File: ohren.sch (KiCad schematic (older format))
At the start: 18 parts

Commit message: Add LEDs and drivers
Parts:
- removed D10, D11, D12, D13, D14, D15, D2, D3, D4, D5, D6, D7, D8, D9: WS2812B, LED_SMD:LED_WS2812B_PLCC4_5.0x5.0mm_P3.2mm, symbol LED:WS2812B
- removed U?: TLC5951RHA, Package_DFN_QFN:Texas_S-PVQFN-N40_EP4.15x4.15mm_ThermalVias, symbol Driver_LED:TLC5951RHA
- added C2, C4: CP, symbol Device:CP
- added C3: C, Capacitor_SMD:C_0805_2012Metric, symbol Device:C
- added D10, D11, D12, D13, D14, D15, D16, D17, D2, D3, D4, D5, D6, D7, D8, D9: LED_ARGB, LED_SMD:LED_Cree-PLCC4_3.2x2.8mm_CCW, symbol Device:LED_ARGB
- added U2: TLC5951RHA, Package_DFN_QFN:Texas_S-PVQFN-N40_EP4.15x4.15mm_ThermalVias, symbol Driver_LED:TLC5951RHA
- C1: footprint LED_SMD:LED_0402_1005Metric -> Capacitor_SMD:C_0805_2012Metric
- gave numbers to parts that had none: 1
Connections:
- net labels added: DCSCHAIN, DCSCK, GND, GSCKB, GSCKG, GSCKR, GSLAT, GSSCHAIN, GSSCK, U1_B0, U1_B1, U1_B2, U1_B3, U1_B4, U1_B5, U1_B6, U1_B7, U1_G0, U1_G1, U1_G2, U1_G3, U1_G4, U1_G5, U1_G6, U1_G7, U1_R0, U1_R1, U1_R2, U1_R3, U1_R4, U1_R5, U1_R6, U1_R7, U2_B0, U2_B1, U2_B2, U2_B3, U2_B4, U2_B5, U2_B6, U2_B7, U2_G0, U2_G1, U2_G2, U2_G3, U2_G4, U2_G5, U2_G6, U2_G7, U2_R0, U2_R1, U2_R2, U2_R3, U2_R4, U2_R5, U2_R6, U2_R7, VCC, VDD, XBLINK
- wire segments 0 -> 158
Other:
- moved on the sheet: D1

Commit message: Route
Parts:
- added C5, C6, C7, C8: C, Capacitor_SMD:C_1210_3225Metric, symbol Device:C
- added J1: Conn_01x14_Male, catear-pcb:solder_conn14, symbol Connector:Conn_01x14_Male
- U1, U2: symbol Driver_LED:TLC5951RHA -> ohren-rescue:TLC5951RHA-Driver_LED
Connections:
- net labels added: DCSIN, DCSOUT, GSSIN, GSSOUT, XBLNK
- net labels removed: XBLINK
- wire segments 158 -> 202
- no-connect marks 0 -> 1
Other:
- moved on the sheet: C1, C2, C3, C4, D1, D10, D11, D12, D13, D14, D15, D16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

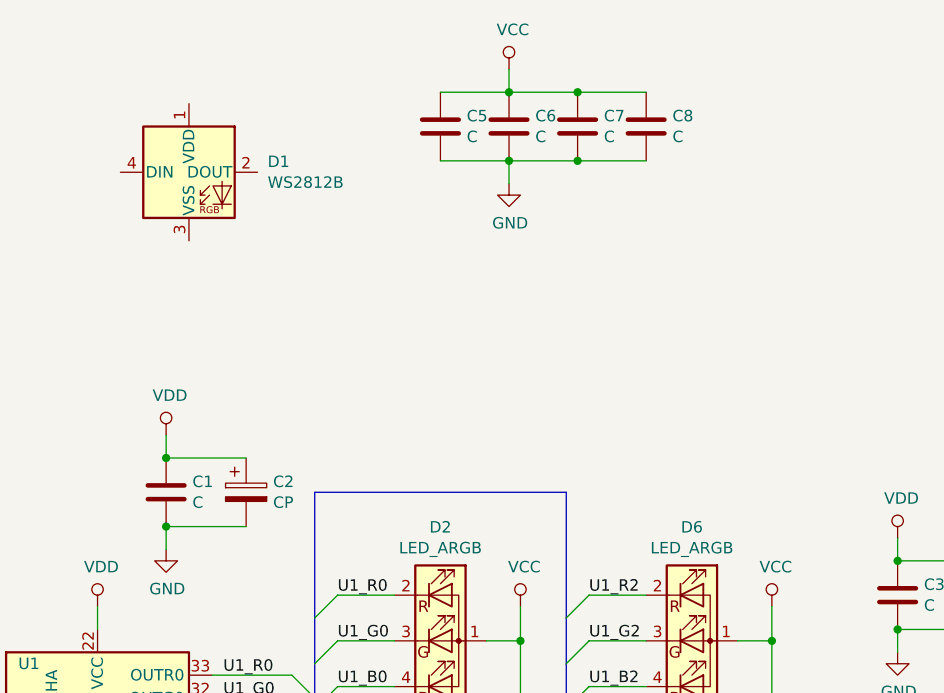
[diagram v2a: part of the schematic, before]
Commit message: Add some bypass capacitance
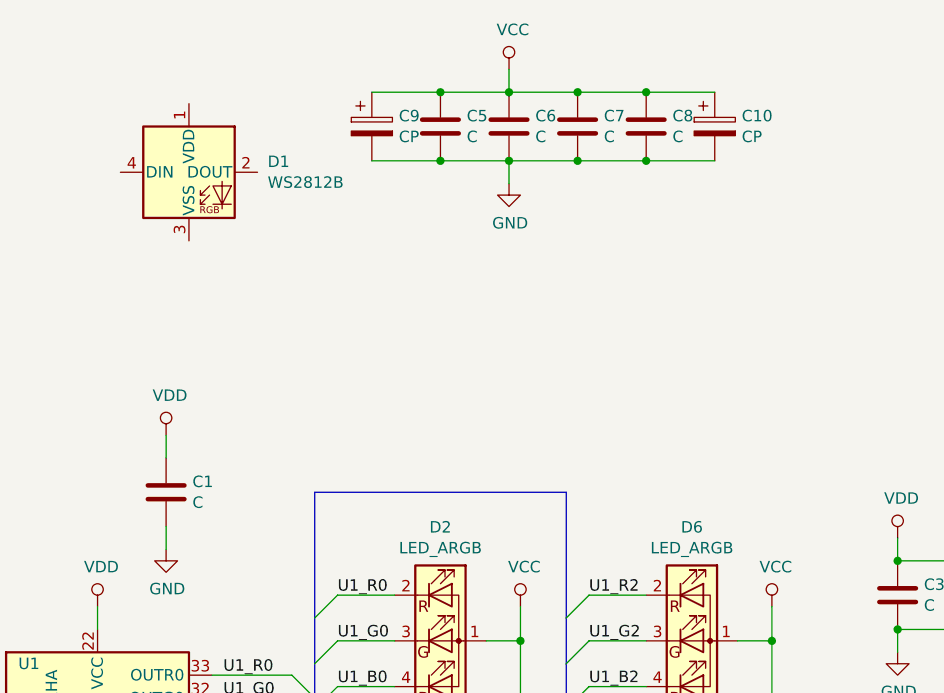
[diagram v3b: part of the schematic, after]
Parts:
- removed C2: CP, symbol Device:CP
- added C10, C9: CP, Capacitor_Tantalum_SMD:CP_EIA-6032-28_Kemet-C, symbol Device:CP
- C4: footprint (none) -> Capacitor_Tantalum_SMD:CP_EIA-6032-28_Kemet-C
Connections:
- net GND: now also C10.2, C9.2
- net VCC: now also C10.1, C9.1
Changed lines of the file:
@@
 Wire Wire Line
 	3350 6150 3350 6250
-Connection ~ 3650 2900
-Wire Wire Line
-	4000 2900 3650 2900
-Connection ~ 3650 2600
-Wire Wire Line
-	4000 2600 3650 2600
-$Comp
-L Device:CP C2
-U 1 1 5C9AA679
-P 4000 2750
-F 0 "C2" H 4118 2796 50  0000 L CNN
-F 1 "CP" H 4118 2705 50  0000 L CNN
-F 2 "" H 4038 2600 50  0001 C CNN
-F 3 "~" H 4000 2750 50  0001 C CNN
-	1    4000 2750
-	1    0    0    -1
-$EndComp
 Wire Wire Line
 	3650 2900 3650 3000
@@
 F 0 "C4" H 7318 3246 50  0000 L CNN
 F 1 "CP" H 7318 3155 50  0000 L CNN
-F 2 "" H 7238 3050 50  0001 C CNN
+F 2 "Capacitor_Tantalum_SMD:CP_EIA-6032-28_Kemet-C" H 7238 3050 50  0001 C CNN
 F 3 "~" H 7200 3200 50  0001 C CNN
 	1    7200 3200
@@
 Wire Wire Line
 	1400 3450 1400 2500
+$Comp
+L Device:CP C9
+U 1 1 5D009474
+P 4550 1150
+F 0 "C9" H 4668 1196 50  0000 L CNN
+F 1 "CP" H 4668 1105 50  0000 L CNN
+F 2 "Capacitor_Tantalum_SMD:CP_EIA-6032-28_Kemet-C" H 4588 1000 50  0001 C CNN
+F 3 "~" H 4550 1150 50  0001 C CNN
+	1    4550 1150
+	1    0    0    -1
+$EndComp
+$Comp
+L Device:CP C10
+U 1 1 5D01A6A4
+P 6050 1150
+F 0 "C10" H 6168 1196 50  0000 L CNN
+F 1 "CP" H 6168 1105 50  0000 L CNN
+F 2 "Capacitor_Tantalum_SMD:CP_EIA-6032-28_Kemet-C" H 6088 1000 50  0001 C CNN
+F 3 "~" H 6050 1150 50  0001 C CNN
+	1    6050 1150
+	1    0    0    -1
+$EndComp
+Wire Wire Line
+	6050 1000 5750 1000
+Connection ~ 5750 1000
+Wire Wire Line
+	6050 1300 5750 1300
+Connection ~ 5750 1300
+Wire Wire Line
+	4850 1000 4550 1000
+Connection ~ 4850 1000
+Wire Wire Line
+	4850 1300 4550 1300
 Wire Bus Line
 	5400 2750 5400 4550
@@
 Wire Bus Line
 	2350 2650 2350 6850
+Connection ~ 4850 1300
 $EndSCHEMATC

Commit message: Partial reroute
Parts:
- removed D1: WS2812B, LED_SMD:LED_WS2812B_PLCC4_5.0x5.0mm_P3.2mm, symbol LED:WS2812B
- removed D13, D16, D2, D3: LED_ARGB, LED_SMD:LED_Cree-PLCC4_3.2x2.8mm_CCW, symbol Device:LED_ARGB
- added D19, D20, D21, D22, D23, D24, D25, D26: LED, catear-pcb:smd_led_universal, symbol Device:LED
- added R1, R2: 2k4, Resistor_SMD:R_0402_1005Metric, symbol Device:R
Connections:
- wire segments 204 -> 227
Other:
- moved on the sheet: D10, D11, D12, D14, D17, D4, D6, D7

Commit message: Reroute finised
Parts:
- removed C4: CP, Capacitor_Tantalum_SMD:CP_EIA-6032-28_Kemet-C, symbol Device:CP
- C10, C9: value CP -> C; footprint Capacitor_Tantalum_SMD:CP_EIA-6032-28_Kemet-C -> Capacitor_SMD:C_1206_3216Metric; symbol Device:CP -> Device:C
- J1: value Conn_01x14_Male -> Conn_01x18_Male; footprint catear-pcb:solder_conn14 -> catear-pcb:solder_conn18; symbol Connector:Conn_01x14_Male -> Connector:Conn_01x18_Male
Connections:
- wire segments 227 -> 242
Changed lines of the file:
@@
 Wire Wire Line
 	7850 6150 7850 6200
-Connection ~ 6850 3350
-Wire Wire Line
-	7200 3350 6850 3350
-Connection ~ 6850 3050
-Wire Wire Line
-	7200 3050 6850 3050
-$Comp
-L Device:CP C4
-U 1 1 5CA31CE6
-P 7200 3200
-F 0 "C4" H 7318 3246 50  0000 L CNN
-F 1 "CP" H 7318 3155 50  0000 L CNN
-F 2 "Capacitor_Tantalum_SMD:CP_EIA-6032-28_Kemet-C" H 7238 3050 50  0001 C CNN
-F 3 "~" H 7200 3200 50  0001 C CNN
-	1    7200 3200
-	1    0    0    -1
-$EndComp
 Wire Wire Line
 	6850 3350 6850 3450
@@
 	1    0    0    -1
 $EndComp
-NoConn ~ 2000 2300
+NoConn ~ 2000 2700
 Wire Wire Line
 	5150 1300 5150 1400
@@
 	1    0    0    -1
 $EndComp
-Wire Wire Line
-	400  2500 400  3200
-$Comp
-L power:GND #PWR0119
-U 1 1 5CC0E0FA
-P 400 3200
-F 0 "#PWR0119" H 400 2950 50  0001 C CNN
-F 1 "GND" H 405 3027 50  0000 C CNN
-F 2 "" H 400 3200 50  0001 C CNN
-F 3 "" H 400 3200 50  0001 C CNN
-	1    400  3200
-	1    0    0    -1
-$EndComp
 $Comp
 L power:VCC #PWR0120
 U 1 1 5CC1AB18
-P 0 2250
-F 0 "#PWR0120" H 0   2100 50  0001 C CNN
-F 1 "VCC" H 17  2423 50  0000 C CNN
-F 2 "" H 0   2250 50  0001 C CNN
-F 3 "" H 0   2250 50  0001 C CNN
-	1    0    2250
-	1    0    0    -1
-$EndComp
-Wire Wire Line
-	0    2250 0    2500
-$Comp
-L power:GND #PWR0121
-U 1 1 5CC4100A
-P 2550 2600
-F 0 "#PWR0121" H 2550 2350 50  0001 C CNN
-F 1 "GND" H 2555 2427 50  0000 C CNN
-F 2 "" H 2550 2600 50  0001 C CNN
-F 3 "" H 2550 2600 50  0001 C CNN
-	1    2550 2600
-	1    0    0    -1
-$EndComp
-Wire Wire Line
-	2550 2600 2550 2500
-Wire Wire Line
-	2550 2500 1500 2500
-Entry Wire Line
-	2250 2750 2350 2650
-Entry Wire Line
-	2250 2850 2350 2750
-Entry Wire Line
-	2250 2950 2350 2850
-Entry Wire Line
-	2250 3050 2350 2950
+P -850 2250
+F 0 "#PWR0120" H -850 2100 50  0001 C CNN
+F 1 "VCC" H -833 2423 50  0000 C CNN
+F 2 "" H -850 2250 50  0001 C CNN
+F 3 "" H -850 2250 50  0001 C CNN
+	1    -850 2250
+	1    0    0    -1
+$EndComp
 Entry Wire Line
 	2250 3150 2350 3050
@@
 Entry Wire Line
 	2250 3750 2350 3650
-Text Label 1800 2850 0    50   ~ 0
+Entry Wire Line
+	2250 3850 2350 3750
+Entry Wire Line
+	2250 3950 2350 3850
+Entry Wire Line
+	2250 4050 2350 3950
+Entry Wire Line
+	2250 4150 2350 4050
+Text Label 1800 4150 0    50   ~ 0
 GSSOUT
-Text Label 1800 2750 0    50   ~ 0
+Text Label 1800 4050 0    50   ~ 0
 DCSOUT
-Text Label 1800 2950 0    50   ~ 0
+Text Label 1800 3450 0    50   ~ 0
 GSSIN
-Text Label 1800 3050 0    50   ~ 0
+Text Label 1800 3350 0    50   ~ 0
 DCSIN
-Text Label 1800 3150 0    50   ~ 0
+Text Label 1800 3550 0    50   ~ 0
 GSSCK
 Text Label 1800 3250 0    50   ~ 0
-GSLAT
-Text Label 1800 3350 0    50   ~ 0
 DCSCK
-Text Label 1800 3450 0    50   ~ 0
+Text Label 1800 3150 0    50   ~ 0
 XBLNK
-Text Label 1800 3550 0    50   ~ 0
+Text Label 1800 3750 0    50   ~ 0
 GSCKR
-Wire Wire Line
-	0    2500 200  2500
-$Comp
-L Connector:Conn_01x14_Male J1
-U 1 1 5CDF8D04
-P 900 2300
-F 0 "J1" V 735 2228 50  0000 C CNN
-F 1 "Conn_01x14_Male" V 826 2228 50  0000 C CNN
-F 2 "catear-pcb:solder_conn14" H 900 2300 50  0001 C CNN
-F 3 "~" H 900 2300 50  0001 C CNN
-	1    900  2300
-	0    1    1    0
-$EndComp
-Connection ~ 200  2500
-Wire Wire Line
-	200  2500 300  2500
-Wire Wire Line
-	-200 2600 -200 2250
-$Comp
-L power:VDD #PWR0122
-U 1 1 5CE5FD09
-P -200 2250
-F 0 "#PWR0122" H -200 2100 50  0001 C CNN
-F 1 "VDD" H -183 2423 50  0000 C CNN
-F 2 "" H -200 2250 50  0001 C CNN
-F 3 "" H -200 2250 50  0001 C CNN
-	1    -200 2250
-	1    0    0    -1
-$EndComp
-Wire Wire Line
-	2250 3650 600  3650
-Wire Wire Line
-	600  3650 600  3550
-Wire Wire Line
-	2250 3750 600  3750
-Wire Wire Line
-	600  3750 600  3650
-Connection ~ 600  3650
-Text Label 1800 3650 0    50   ~ 0
+Text Label 1800 3850 0    50   ~ 0
 GSCKG
-Text Label 1800 3750 0    50   ~ 0
+Text Label 1800 3950 0    50   ~ 0
 GSCKB
 Entry Wire Line
@@
 Entry Wire Line
 	2350 4350 2450 4250
-Wire Wire Line
-	500  3050 2250 3050
-Wire Wire Line
-	500  2500 500  3050
-Wire Wire Line
-	600  2950 600  2500
-Wire Wire Line
-	600  2950 2250 2950
-Wire Wire Line
-	600  3550 1000 3550
-Wire Wire Line
-	700  2850 700  2500
-Wire Wire Line
-	700  2850 2250 2850
-Wire Wire Line
-	800  2750 800  2500
-Wire Wire Line
-	800  2750 2250 2750
-Wire Wire Line
-	-200 2600 900  2600
-Wire Wire Line
-	900  2600 900  2500
-Wire Wire Line
-	1000 2500 1000 3550
-Connection ~ 1000 3550
-Wire Wire Line
-	1000 3550 2250 3550
-Wire Wire Line
-	2250 3250 1100 3250
-Wire Wire Line
-	1100 3250 1100 2500
-Wire Wire Line
-	2250 3150 1200 3150
-Wire Wire Line
-	1200 3150 1200 2500
-Wire Wire Line
-	2250 3350 1300 3350
-Wire Wire Line
-	1300 3350 1300 2500
-Wire Wire Line
-	2250 3450 1400 3450
-Wire Wire Line
-	1400 3450 1400 2500
-$Comp
-L Device:CP C9
+$Comp
+L Device:C C9
 U 1 1 5D009474
 P 4550 1150
 F 0 "C9" H 4668 1196 50  0000 L CNN
-F 1 "CP" H 4668 1105 50  0000 L CNN
-F 2 "Capacitor_Tantalum_SMD:CP_EIA-6032-28_Kemet-C" H 4588 1000 50  0001 C CNN
+F 1 "C" H 4668 1105 50  0000 L CNN
+F 2 "Capacitor_SMD:C_1206_3216Metric" H 4588 1000 50  0001 C CNN
 F 3 "~" H 4550 1150 50  0001 C CNN
 	1    4550 1150
@@
 $EndComp
 $Comp
-L Device:CP C10
+L Device:C C10
 U 1 1 5D01A6A4
 P 6050 1150
 F 0 "C10" H 6168 1196 50  0000 L CNN
-F 1 "CP" H 6168 1105 50  0000 L CNN
-F 2 "Capacitor_Tantalum_SMD:CP_EIA-6032-28_Kemet-C" H 6088 1000 50  0001 C CNN
+F 1 "C" H 6168 1105 50  0000 L CNN
+F 2 "Capacitor_SMD:C_1206_3216Metric" H 6088 1000 50  0001 C CNN
 F 3 "~" H 6050 1150 50  0001 C CNN
 	1    6050 1150
@@
 Wire Wire Line
 	2800 1500 2800 1750
+Text Label 3100 1750 1    50   ~ 0
+U2_G1
+Wire Wire Line
+	3100 1500 3100 1750
+Text Label 2500 1750 1    50   ~ 0
+U2_R1
+Wire Wire Line
+	2500 1500 2500 1750
+$Comp
+L Connector:Conn_01x18_Male J1
+U 1 1 5CDF8D04
+P 550 2200
+F 0 "J1" V 385 2128 50  0000 C CNN
+F 1 "Conn_01x18_Male" V 476 2128 50  0000 C CNN
+F 2 "catear-pcb:solder_conn18" H 550 2200 50  0001 C CNN
+F 3 "~" H 550 2200 50  0001 C CNN
+	1    550  2200
+	0    1    1    0
+$EndComp
+Wire Wire Line
+	-350 2400 -350 2550
+Wire Wire Line
+	-350 2550 -850 2550
+Wire Wire Line
+	-850 2550 -850 2250
+Wire Wire Line
+	-350 2550 -250 2550
+Wire Wire Line
+	-250 2550 -250 2400
+Connection ~ -350 2550
+$Comp
+L power:VCC #PWR0119
+U 1 1 5CD6CF6B
+P 1800 2250
+F 0 "#PWR0119" H 1800 2100 50  0001 C CNN
+F 1 "VCC" H 1817 2423 50  0000 C CNN
+F 2 "" H 1800 2250 50  0001 C CNN
+F 3 "" H 1800 2250 50  0001 C CNN
+	1    1800 2250
+	1    0    0    -1
+$EndComp
+Wire Wire Line
+	1800 2550 1800 2250
+Wire Wire Line
+	1800 2550 1350 2550
+Wire Wire Line
+	1250 2550 1250 2400
+Wire Wire Line
+	1350 2400 1350 2550
+Connection ~ 1350 2550
+Wire Wire Line
+	1350 2550 1250 2550
+Wire Wire Line
+	-150 2400 -150 2650
+Wire Wire Line
+	-150 2650 -850 2650
+Wire Wire Line
+	-50  2400 -50  2650
+Wire Wire Line
+	-50  2650 -150 2650
+Connection ~ -150 2650
+$Comp
+L power:GND #PWR0121
+U 1 1 5CDDA28F
+P -850 2750
+F 0 "#PWR0121" H -850 2500 50  0001 C CNN
+F 1 "GND" H -845 2577 50  0000 C CNN
+F 2 "" H -850 2750 50  0001 C CNN
+F 3 "" H -850 2750 50  0001 C CNN
+	1    -850 2750
+	1    0    0    -1
+$EndComp
+Wire Wire Line
+	-850 2750 -850 2650
+$Comp
+L power:GND #PWR0124
+U 1 1 5CDEC54B
+P 1800 2850
+F 0 "#PWR0124" H 1800 2600 50  0001 C CNN
+F 1 "GND" H 1805 2677 50  0000 C CNN
+F 2 "" H 1800 2850 50  0001 C CNN
+F 3 "" H 1800 2850 50  0001 C CNN
+	1    1800 2850
+	1    0    0    -1
+$EndComp
+Wire Wire Line
+	1800 2850 1800 2750
+Wire Wire Line
+	1800 2750 1150 2750
+Connection ~ 1150 2750
+Wire Wire Line
+	1150 2750 1050 2750
+$Comp
+L power:VDD #PWR0122
+U 1 1 5CE3A90D
+P 2000 2250
+F 0 "#PWR0122" H 2000 2100 50  0001 C CNN
+F 1 "VDD" H 2017 2423 50  0000 C CNN
+F 2 "" H 2000 2250 50  0001 C CNN
+F 3 "" H 2000 2250 50  0001 C CNN
+	1    2000 2250
+	1    0    0    -1
+$EndComp
+Wire Wire Line
+	1150 2400 1150 2750
+Wire Wire Line
+	1050 2400 1050 2750
+Wire Wire Line
+	2000 2650 950  2650
+Wire Wire Line
+	950  2650 950  2400
+Wire Wire Line
+	2000 2250 2000 2650
+Wire Wire Line
+	2250 3150 850  3150
+Wire Wire Line
+	850  3150 850  2400
+Wire Wire Line
+	2250 3250 750  3250
+Wire Wire Line
+	750  3250 750  2400
+Text Label 1800 3650 0    50   ~ 0
+GSLAT
+Wire Wire Line
+	2250 3350 650  3350
+Wire Wire Line
+	650  3350 650  2400
+Wire Wire Line
+	2250 3450 550  3450
+Wire Wire Line
+	550  3450 550  2400
+Wire Wire Line
+	2250 3550 450  3550
+Wire Wire Line
+	450  3550 450  2400
+Wire Wire Line
+	2250 3650 350  3650
+Wire Wire Line
+	350  3650 350  2400
+Wire Wire Line
+	2250 3750 250  3750
+Wire Wire Line
+	250  3750 250  2400
+Wire Wire Line
+	2250 3850 250  3850
+Wire Wire Line
+	250  3850 250  3750
+Connection ~ 250  3750
+Wire Wire Line
+	2250 3950 250  3950
+Wire Wire Line
+	250  3950 250  3850
+Connection ~ 250  3850
+Wire Wire Line
+	2250 4050 150  4050
+Wire Wire Line
+	150  4050 150  2400
+Wire Wire Line
+	2250 4150 50   4150
+Wire Wire Line
+	50   4150 50   2400
+Text Label 1900 1750 1    50   ~ 0
+U2_B4
+Wire Wire Line
+	1900 1500 1900 1750
+Text Label 2200 1750 1    50   ~ 0
+U2_R4
+Wire Wire Line
+	2200 1500 2200 1750
 Wire Bus Line
 	5400 2750 5400 4550
@@
 	8800 4950 8800 6500
 Wire Bus Line
-	2350 2650 2350 6850
+	2350 3050 2350 6850
 $EndSCHEMATC

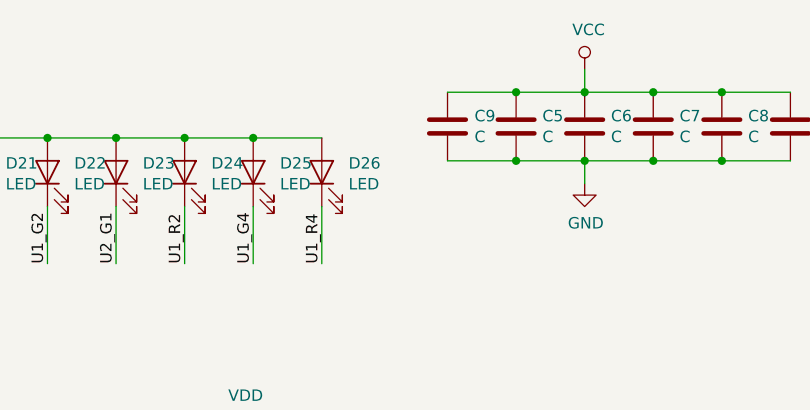
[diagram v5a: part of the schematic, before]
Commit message: Add additional VIA stitching and bypass capacitance
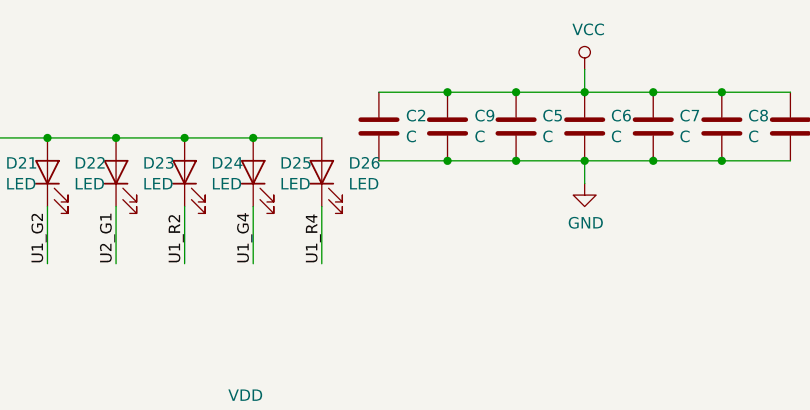
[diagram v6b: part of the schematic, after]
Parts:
- added C2: C, Capacitor_SMD:C_1210_3225Metric, symbol Device:C
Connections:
- wire segments 242 -> 244
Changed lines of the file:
@@
 Wire Wire Line
 	2200 1500 2200 1750
+$Comp
+L Device:C C2
+U 1 1 5D1B5671
+P 4250 1150
+F 0 "C2" H 4368 1196 50  0000 L CNN
+F 1 "C" H 4368 1105 50  0000 L CNN
+F 2 "Capacitor_SMD:C_1210_3225Metric" H 4288 1000 50  0001 C CNN
+F 3 "~" H 4250 1150 50  0001 C CNN
+	1    4250 1150
+	1    0    0    -1
+$EndComp
+Wire Wire Line
+	4550 1000 4250 1000
+Wire Wire Line
+	4550 1300 4250 1300
 Wire Bus Line
 	5400 2750 5400 4550
@@
 Wire Bus Line
 	2350 3050 2350 6850
+Connection ~ 4550 1000
+Connection ~ 4550 1300
 $EndSCHEMATC

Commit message: Switch to LEDs with integrated controller
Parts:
- removed C3: C, Capacitor_SMD:C_0805_2012Metric, symbol Device:C
- removed D10, D11, D12, D14, D15, D17, D4, D5, D6, D7, D8, D9: LED_ARGB, LED_SMD:LED_Cree-PLCC4_3.2x2.8mm_CCW, symbol Device:LED_ARGB
- removed R2: 2k4, Resistor_SMD:R_0402_1005Metric, symbol Device:R
- removed U2: TLC5951RHA, Package_DFN_QFN:Texas_S-PVQFN-N40_EP4.15x4.15mm_ThermalVias, symbol ohren-rescue:TLC5951RHA-Driver_LED
- added D1, D10, D11, D12, D13, D14, D15, D16, D17, D18, D2, D27, D28, D29, D3, D30, D31, D32, D33, D34, D35, D36, D37, D38, D39, D4, D40, D41, D42, D43, D44, D45, D46, D47, D5, D6, D7, D8, D9: SK6812MINI-1515, catear-pcb:LED_1515_4, symbol sk6812mini-1515:SK6812MINI-1515
- added D48, D49, D50, D51, D52, D53, D54, D55, D56, D57, D58, D59, D60, D61, D62, D63: LED, catear-pcb:smd_led_universal, symbol Device:LED
- J1: value Conn_01x18_Male -> Conn_01x19_Male; footprint catear-pcb:solder_conn18 -> catear-pcb:Molex_Easy-On_54550-1971_1x19_P0.5mm_Horizontal; symbol Connector:Conn_01x18_Male -> Connector:Conn_01x19_Male
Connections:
- net labels added: DIN, DLINK0, DLINK1
- net labels removed: DCSCHAIN, GSSCHAIN, U2_B0, U2_B1, U2_B2, U2_B3, U2_B4, U2_B5, U2_B6, U2_B7, U2_G0, U2_G1, U2_G3, U2_G4, U2_G5, U2_G6, U2_G7, U2_R0, U2_R1, U2_R3, U2_R4, U2_R5, U2_R6, U2_R7
- wire segments 244 -> 379
- no-connect marks 1 -> 0
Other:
- moved on the sheet: C1, C10, C2, C5, C6, C7, C8, C9, D19, D20, D21, D22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
